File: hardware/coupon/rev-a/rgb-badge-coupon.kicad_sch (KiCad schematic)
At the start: 0 parts

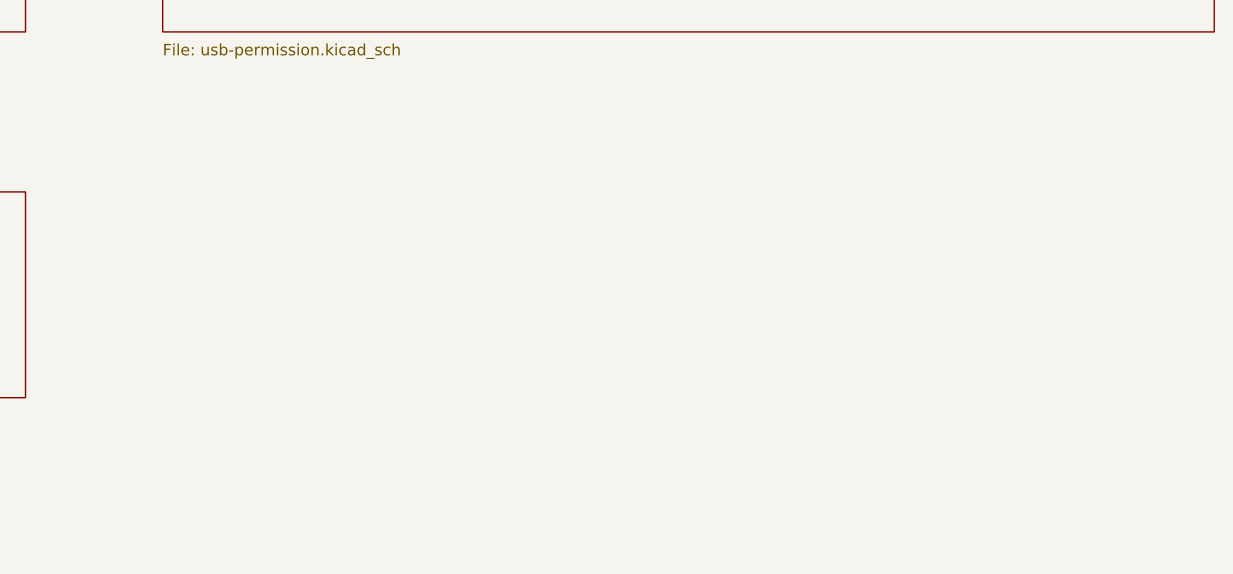
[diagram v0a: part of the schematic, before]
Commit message: Connect provisional BQ24074 charger core to battery NTC
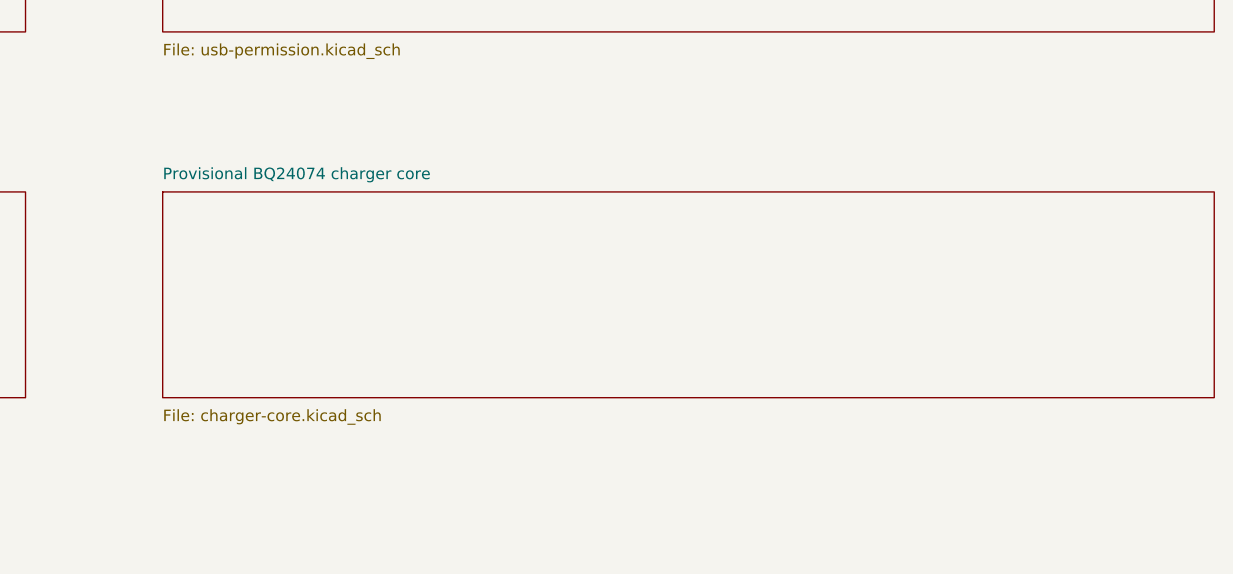
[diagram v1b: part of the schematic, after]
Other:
- added sheet Provisional BQ24074 charger core (charger-core.kicad_sch)
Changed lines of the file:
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@@
 (property "Sheetfile" "charger-temperature.kicad_sch" (at 152.40 257.81 0) (effects (font (size 1.27 1.27)) (justify left top)))
 (instances (project "rgb-badge-coupon" (path "/207fb68e-2ddb-46bb-8712-eba2f8c5eef6" (page "15")))))
+(sheet (at 284.48 233.68) (size 116.84 22.86)
+(exclude_from_sim no) (in_bom yes) (on_board yes) (dnp no)
+(stroke (width 0.1524) (type solid)) (fill (color 0 0 0 0))
+(property "Sheetname" "Provisional BQ24074 charger core" (at 284.48 232.41 0) (effects (font (size 1.27 1.27)) (justify left bottom)))
+(property "Sheetfile" "charger-core.kicad_sch" (at 284.48 257.81 0) (effects (font (size 1.27 1.27)) (justify left top)))
+(instances (project "rgb-badge-coupon" (path "/207fb68e-2ddb-46bb-8712-eba2f8c5eef6" (page "16")))))
 (sheet_instances (path "/" (page "1")))
 (embedded_fonts no)

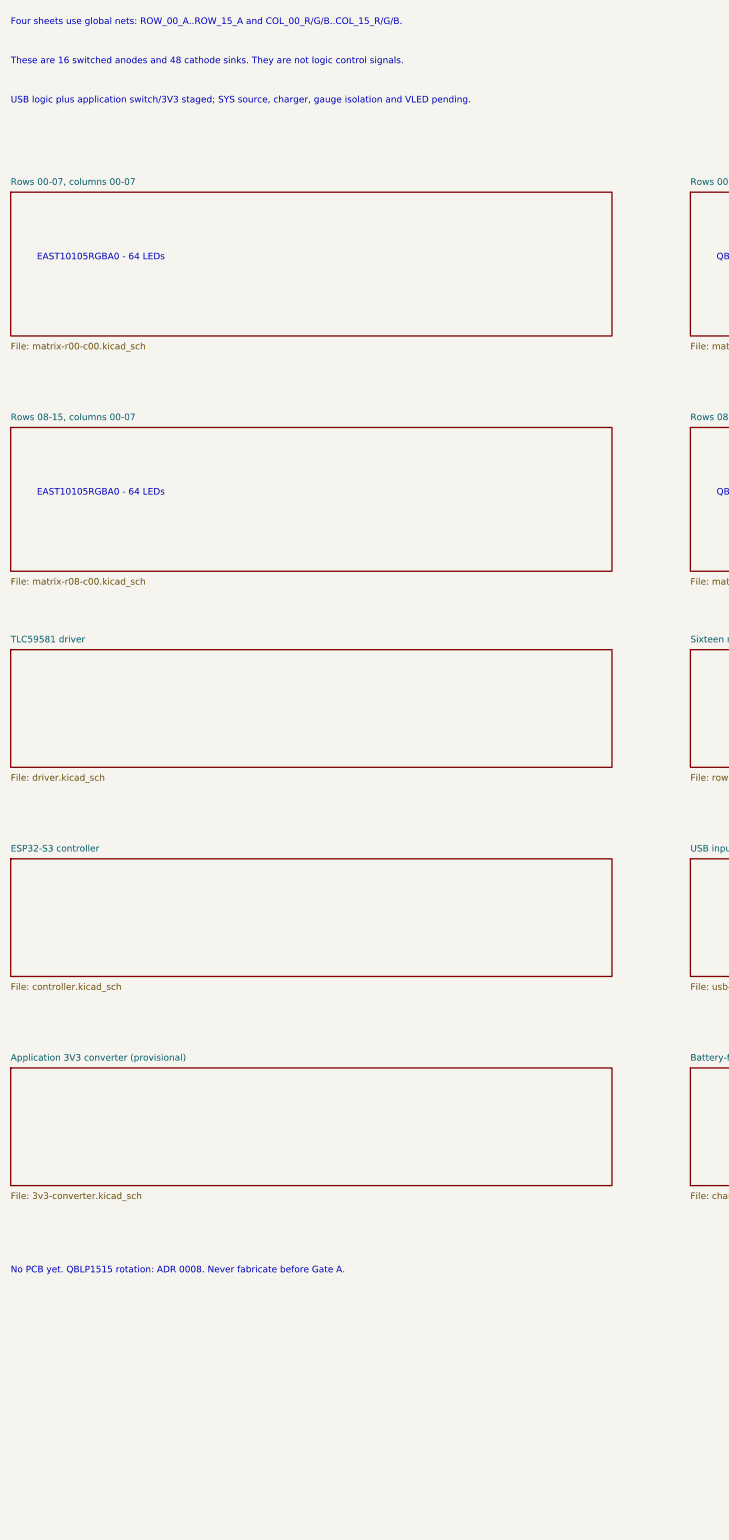
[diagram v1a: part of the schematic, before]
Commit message: Capture provisional E1 charger gate with independent hardware inhibits
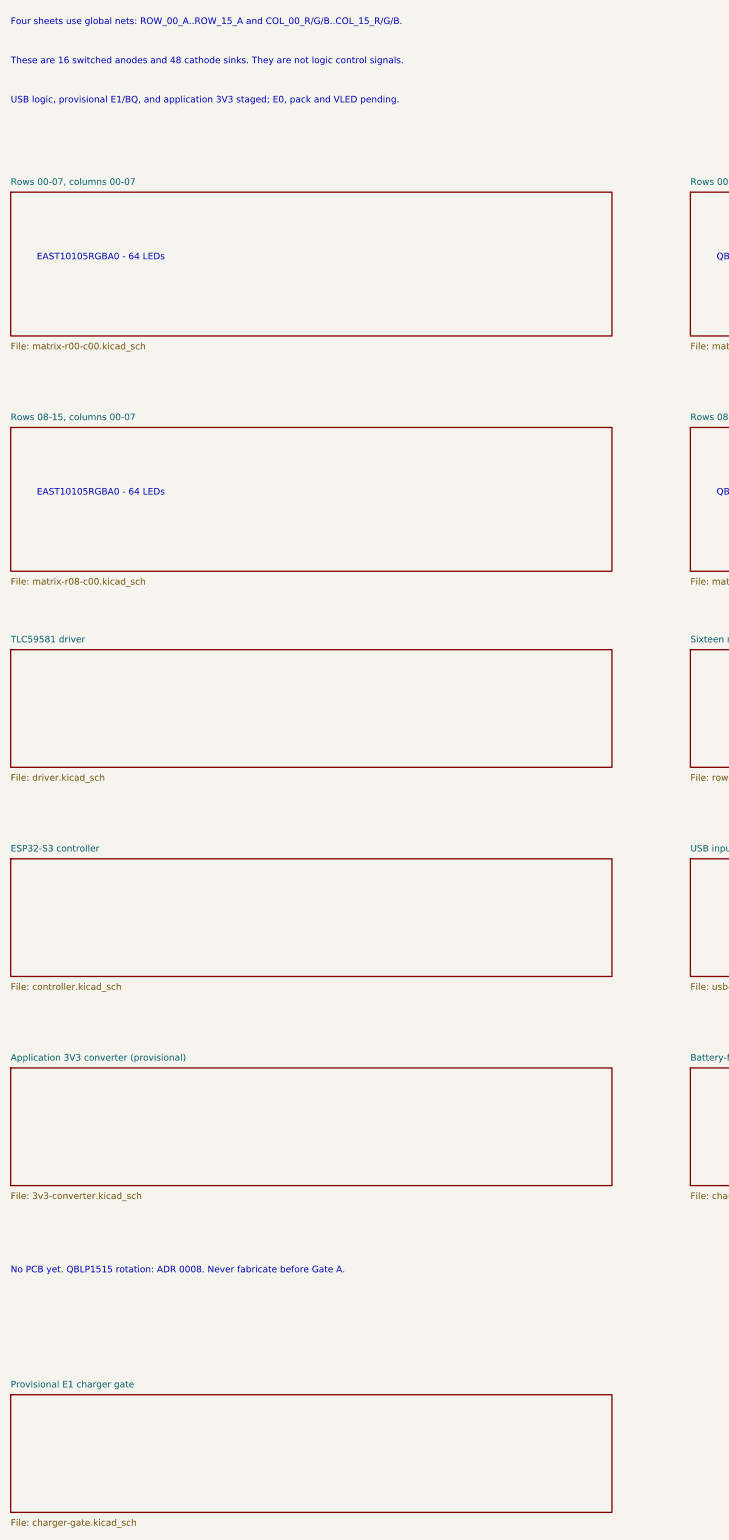
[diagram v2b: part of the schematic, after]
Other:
- added sheet Provisional E1 charger gate (charger-gate.kicad_sch)
- note added: "USB logic, provisional E1/BQ, and application 3V3 staged; E0, pack and VLED pending."
- note removed: "USB logic plus application switch/3V3 staged; SYS source, charger, gauge isolation and VLED pending."
- title: Coupon Rev A - display, USB and provisional application power -> Coupon Rev A - display, USB and provisional power
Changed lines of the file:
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@@
 (generator "rgb_badge_matrix")
 (generator_version "1.0")
-(paper "A3")
-(title_block (title "Coupon Rev A - display, USB and provisional application power") (rev "A-draft") (comment 1 "SPDX-License-Identifier: CERN-OHL-S-2.0") (comment 2 "Input protection, charger, gauge switch and VLED power pending"))
+(paper "A2")
+(title_block (title "Coupon Rev A - display, USB and provisional power") (rev "A-draft") (comment 1 "SPDX-License-Identifier: CERN-OHL-S-2.0") (comment 2 "E0 input protection, pack, gauge switch and VLED pending"))
 (text "16 x 16 RGB matrix, TLC59581 driver, row selectors and ESP32-S3 controller" (at 20.32 20.32 0) (effects (font (size 2.0 2.0)) (justify left)))
 (text "Four sheets use global nets: ROW_00_A..ROW_15_A and COL_00_R/G/B..COL_15_R/G/B." (at 20.32 30.48 0) (effects (font (size 1.27 1.27)) (justify left)))
 (text "These are 16 switched anodes and 48 cathode sinks. They are not logic control signals." (at 20.32 38.10 0) (effects (font (size 1.27 1.27)) (justify left)))
-(text "USB logic plus application switch/3V3 staged; SYS source, charger, gauge isolation and VLED pending." (at 20.32 45.72 0) (effects (font (size 1.27 1.27)) (justify left)))
+(text "USB logic, provisional E1/BQ, and application 3V3 staged; E0, pack and VLED pending." (at 20.32 45.72 0) (effects (font (size 1.27 1.27)) (justify left)))
 (text "No PCB yet. QBLP1515 rotation: ADR 0008. Never fabricate before Gate A." (at 20.32 273.05 0) (effects (font (size 1.27 1.27)) (justify left)))
 (sheet (at 20.32 63.50) (size 116.84 27.94)
@@
 (property "Sheetfile" "charger-core.kicad_sch" (at 284.48 257.81 0) (effects (font (size 1.27 1.27)) (justify left top)))
 (instances (project "rgb-badge-coupon" (path "/207fb68e-2ddb-46bb-8712-eba2f8c5eef6" (page "16")))))
+(sheet (at 20.32 297.18) (size 116.84 22.86)
+(exclude_from_sim no) (in_bom yes) (on_board yes) (dnp no)
+(stroke (width 0.1524) (type solid)) (fill (color 0 0 0 0))
+(property "Sheetname" "Provisional E1 charger gate" (at 20.32 295.91 0) (effects (font (size 1.27 1.27)) (justify left bottom)))
+(property "Sheetfile" "charger-gate.kicad_sch" (at 20.32 321.31 0) (effects (font (size 1.27 1.27)) (justify left top)))
+(instances (project "rgb-badge-coupon" (path "/207fb68e-2ddb-46bb-8712-eba2f8c5eef6" (page "17")))))
 (sheet_instances (path "/" (page "1")))
 (embedded_fonts no)

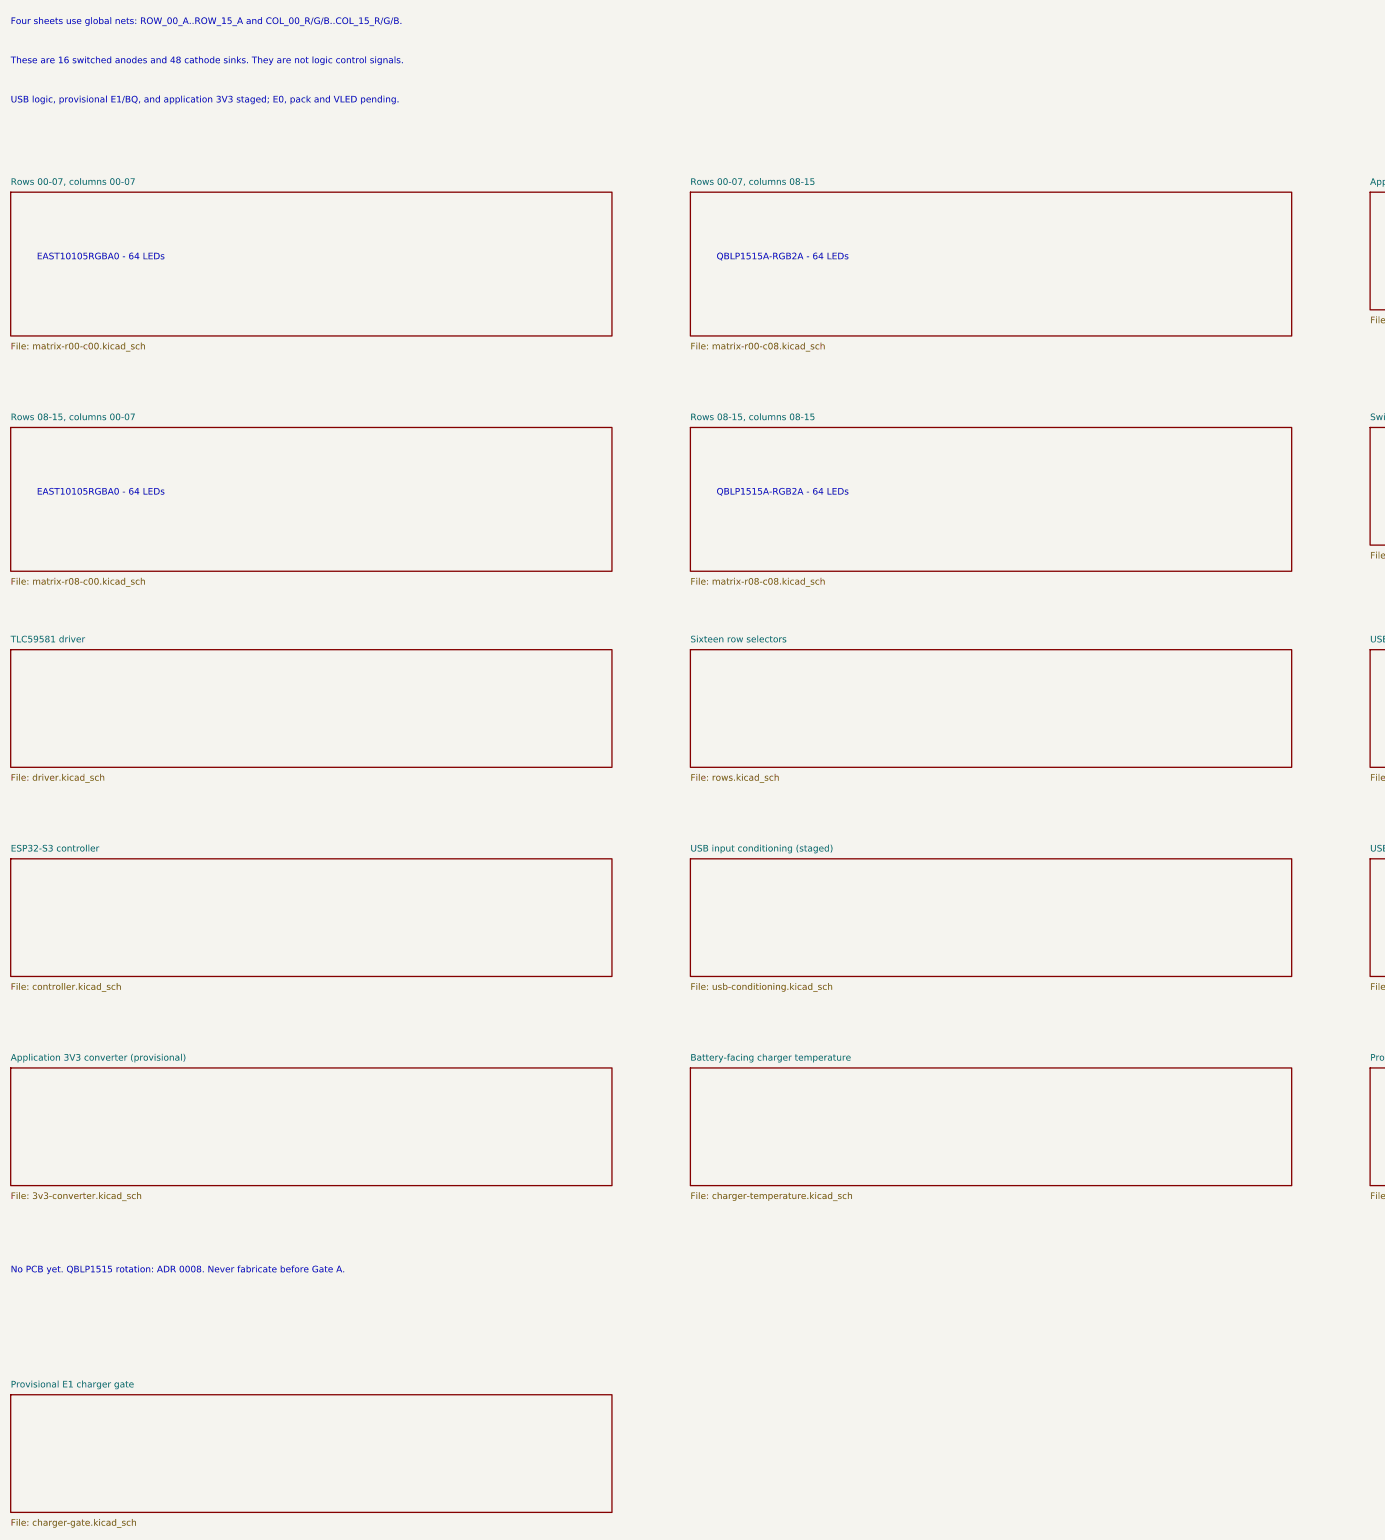
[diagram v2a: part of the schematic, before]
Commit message: Capture provisional E0 protected USB source bridge
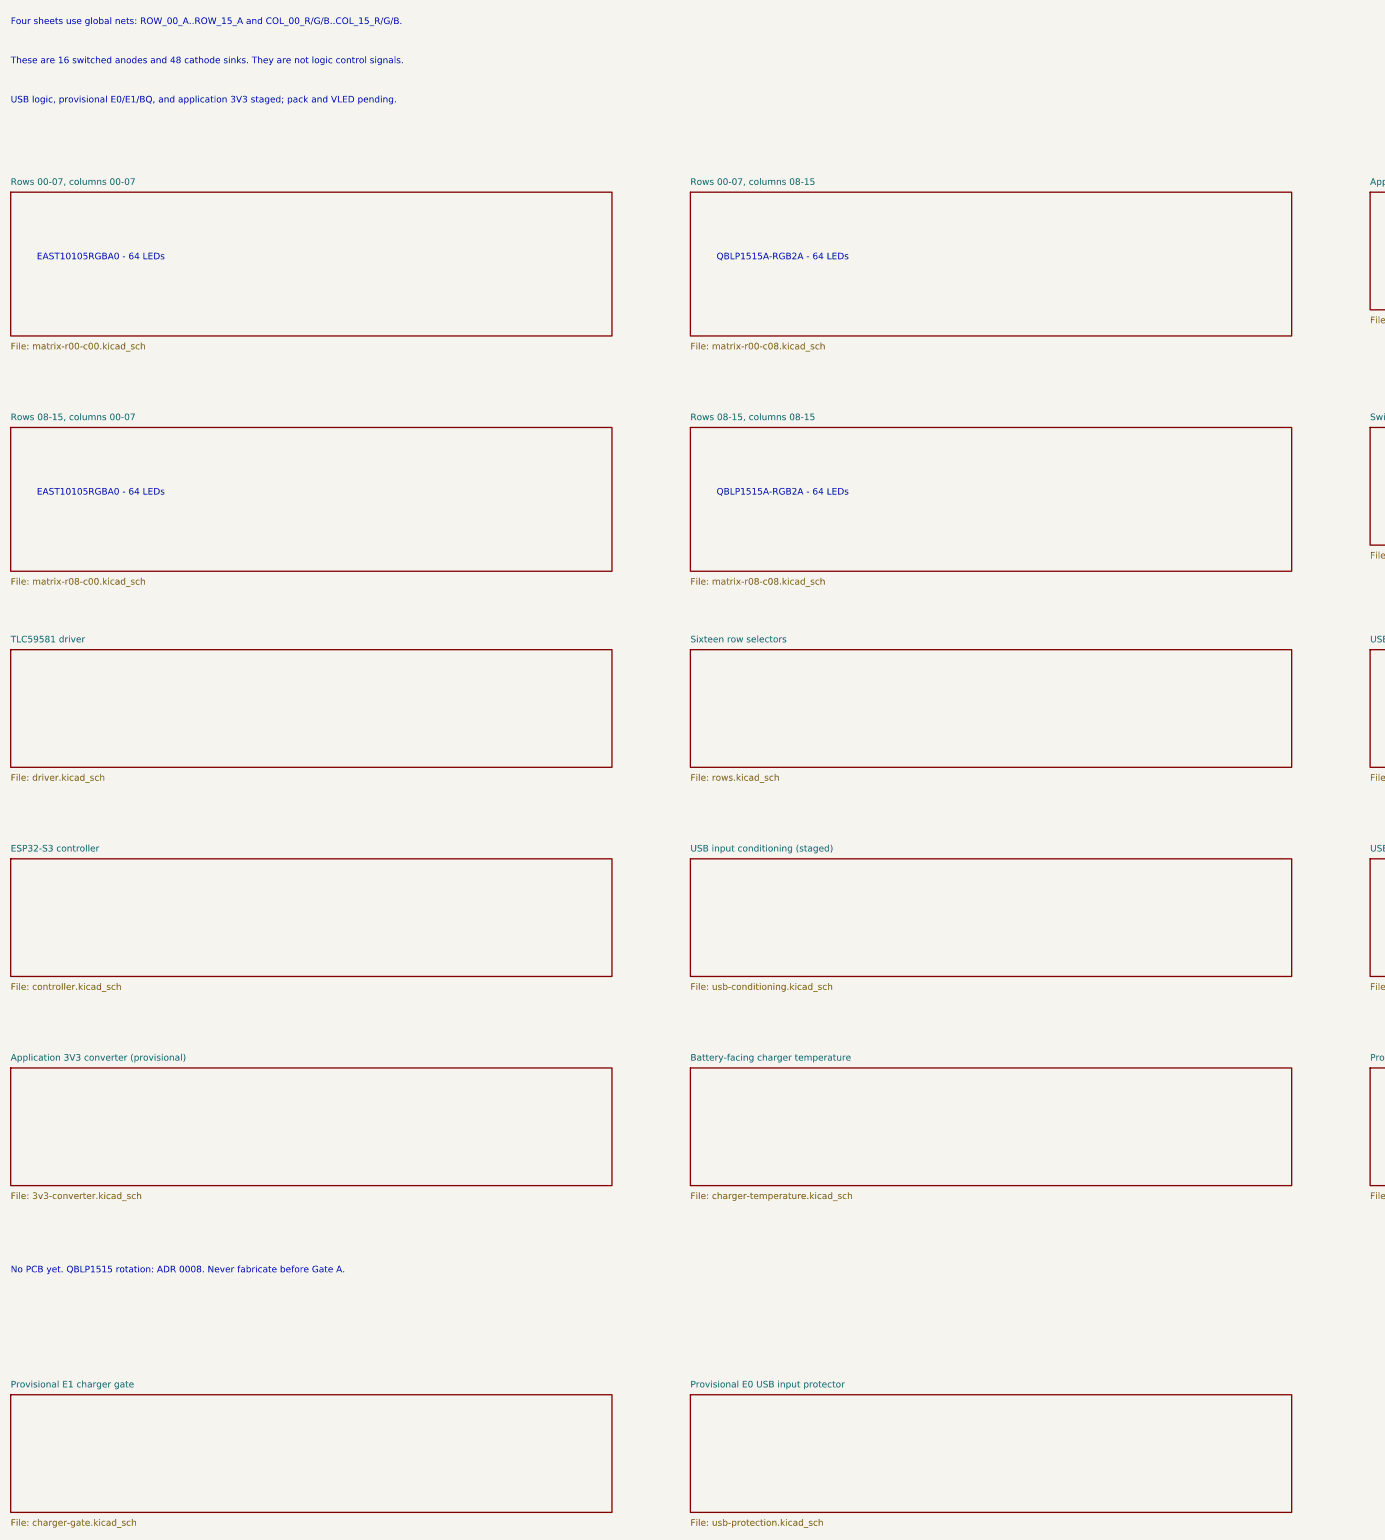
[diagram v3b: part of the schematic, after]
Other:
- added sheet Provisional E0 USB input protector (usb-protection.kicad_sch)
- note added: "USB logic, provisional E0/E1/BQ, and application 3V3 staged; pack and VLED pending."
- note removed: "USB logic, provisional E1/BQ, and application 3V3 staged; E0, pack and VLED pending."
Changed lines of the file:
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@@
 (generator_version "1.0")
 (paper "A2")
-(title_block (title "Coupon Rev A - display, USB and provisional power") (rev "A-draft") (comment 1 "SPDX-License-Identifier: CERN-OHL-S-2.0") (comment 2 "E0 input protection, pack, gauge switch and VLED pending"))
+(title_block (title "Coupon Rev A - display, USB and provisional power") (rev "A-draft") (comment 1 "SPDX-License-Identifier: CERN-OHL-S-2.0") (comment 2 "Pack, gauge switch and VLED pending; E0/E1 unqualified"))
 (text "16 x 16 RGB matrix, TLC59581 driver, row selectors and ESP32-S3 controller" (at 20.32 20.32 0) (effects (font (size 2.0 2.0)) (justify left)))
 (text "Four sheets use global nets: ROW_00_A..ROW_15_A and COL_00_R/G/B..COL_15_R/G/B." (at 20.32 30.48 0) (effects (font (size 1.27 1.27)) (justify left)))
 (text "These are 16 switched anodes and 48 cathode sinks. They are not logic control signals." (at 20.32 38.10 0) (effects (font (size 1.27 1.27)) (justify left)))
-(text "USB logic, provisional E1/BQ, and application 3V3 staged; E0, pack and VLED pending." (at 20.32 45.72 0) (effects (font (size 1.27 1.27)) (justify left)))
+(text "USB logic, provisional E0/E1/BQ, and application 3V3 staged; pack and VLED pending." (at 20.32 45.72 0) (effects (font (size 1.27 1.27)) (justify left)))
 (text "No PCB yet. QBLP1515 rotation: ADR 0008. Never fabricate before Gate A." (at 20.32 273.05 0) (effects (font (size 1.27 1.27)) (justify left)))
 (sheet (at 20.32 63.50) (size 116.84 27.94)
@@
 (property "Sheetfile" "charger-gate.kicad_sch" (at 20.32 321.31 0) (effects (font (size 1.27 1.27)) (justify left top)))
 (instances (project "rgb-badge-coupon" (path "/207fb68e-2ddb-46bb-8712-eba2f8c5eef6" (page "17")))))
+(sheet (at 152.40 297.18) (size 116.84 22.86)
+(exclude_from_sim no) (in_bom yes) (on_board yes) (dnp no)
+(stroke (width 0.1524) (type solid)) (fill (color 0 0 0 0))
+(property "Sheetname" "Provisional E0 USB input protector" (at 152.40 295.91 0) (effects (font (size 1.27 1.27)) (justify left bottom)))
+(property "Sheetfile" "usb-protection.kicad_sch" (at 152.40 321.31 0) (effects (font (size 1.27 1.27)) (justify left top)))
+(instances (project "rgb-badge-coupon" (path "/207fb68e-2ddb-46bb-8712-eba2f8c5eef6" (page "18")))))
 (sheet_instances (path "/" (page "1")))
 (embedded_fonts no)
